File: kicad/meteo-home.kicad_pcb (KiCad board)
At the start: 2 copper layers, 37.5 x 51.4 mm, 14 parts, among them U1 WeMos_D1_mini, U2 SGP30

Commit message: Better connection process control
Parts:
- removed REF** (x4): MountingHole_2.2mm_M2, Mounting_Holes:MountingHole_2.2mm_M2
- moved U2 8.22 mm to (132.2, 96.6), turned to 90 degrees
- moved DHT22 2.09 mm to (121.8, 95.6), turned to 0 degrees
- moved R4 1.70 mm to (110.8, 91.8)
- renumbered D3 to G, D1 to R, D2 to Y
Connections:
- U2 pad 3: Net-(U1-Pad14) -> Net-(U1-Pad13)
- U2 pad 4: Net-(U1-Pad13) -> Net-(U1-Pad14)
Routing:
- net Net-(R4-Pad2): track 63.6 -> 74.3 mm
- net /5V: track 20.9 -> 14.4 mm
- net Net-(U1-Pad14): track 12.5 -> 17.4 mm
- net Net-(U1-Pad13): track 12.5 -> 16.1 mm
- net /3.3V: track 42.8 -> 39.7 mm
- net /GND: track 95.5 -> 96.3 mm
- removed copper zone on B.Cu, net /GND
- removed copper zone on F.Cu, net /GND
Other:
- board text added: "CO2 Detector https://github.com/deuteros76/co2-detector"
- board text removed: "Meteo-home https://github.com/deuteros76/meteo-home"

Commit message: fix: board updated to the last one used in co2-detector
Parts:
- added REF**: MountingHole_2.2mm_M2, Mounting_Holes:MountingHole_2.2mm_M2, F.Cu at (138.0, 93.2)
- added REF**: MountingHole_2.2mm_M2, Mounting_Holes:MountingHole_2.2mm_M2, F.Cu at (139.4, 52.4)
- added REF**: MountingHole_2.2mm_M2, Mounting_Holes:MountingHole_2.2mm_M2, F.Cu at (107.6, 52.4)
- moved U2 1.72 mm to (131.2, 98.0)
- moved DHT22 1.60 mm to (120.2, 95.6)
- moved R4 0.60 mm to (110.2, 91.8)
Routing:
- net /3.3V: track 39.7 -> 53.1 mm
- net Net-(R4-Pad2): track 74.3 -> 61.5 mm
- net /GND: track 96.3 -> 85.9 mm
- net Net-(U1-Pad14): track 17.4 -> 15.8 mm
- net Net-(U1-Pad13): track 16.1 -> 15.1 mm
- added copper zone on B.Cu, net /GND
- added copper zone on F.Cu, net /GND
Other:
- board text added: "CO2 Detector Rev 2 https://github.com/deuteros76/co2-detector"
- board text removed: "CO2 Detector https://github.com/deuteros76/co2-detector"

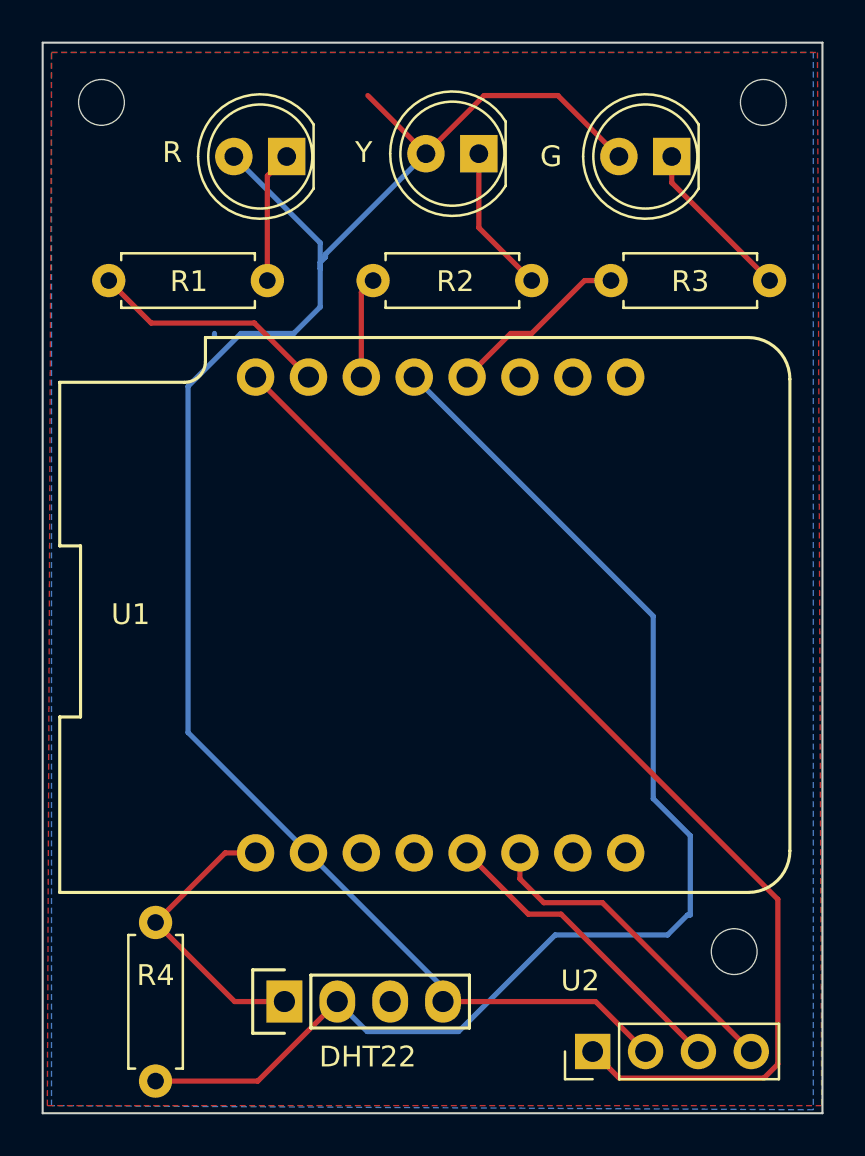
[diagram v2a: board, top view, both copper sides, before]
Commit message: fix: allow deep sleep conecting RST and D0
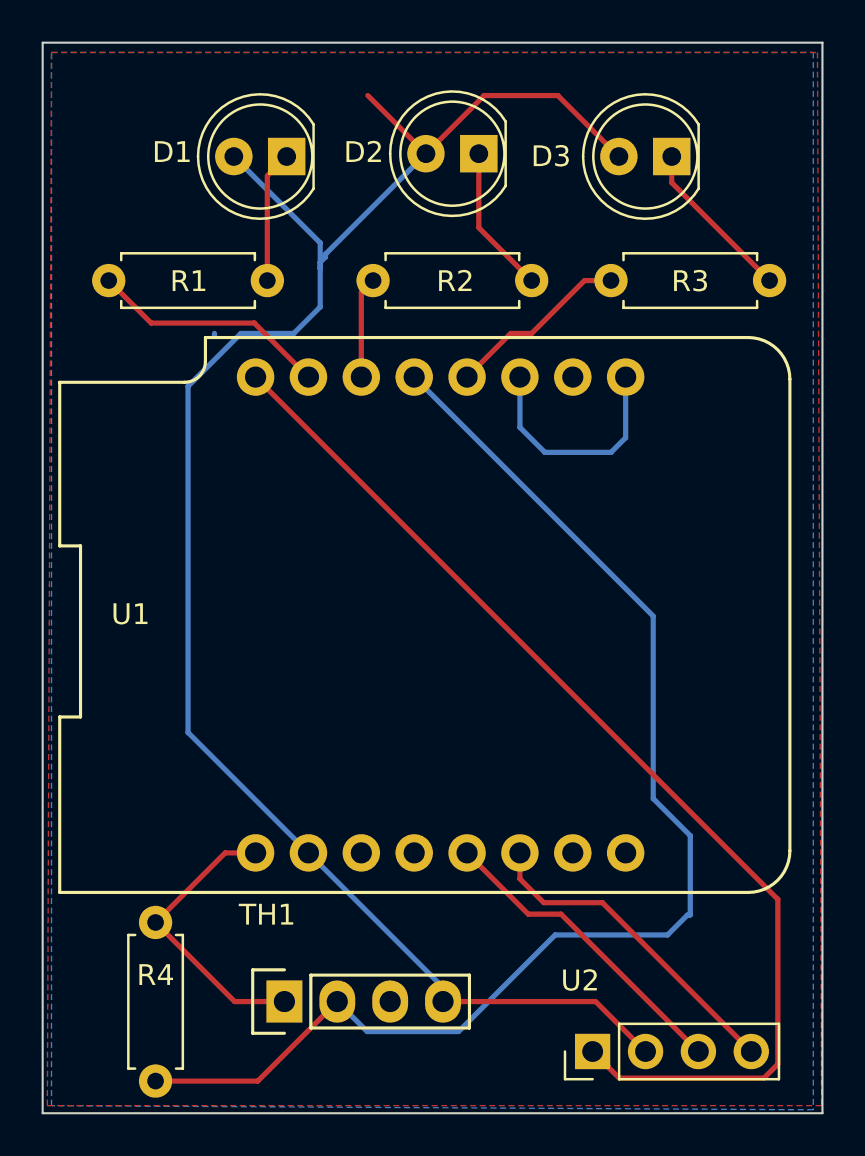
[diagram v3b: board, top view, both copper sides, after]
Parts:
- removed REF** (x3): MountingHole_2.2mm_M2, Mounting_Holes:MountingHole_2.2mm_M2
- TH1: renamed from DHT22; value DHT22_Temperature_Humidity -> DHT22
- renumbered R to D1, Y to D2, G to D3
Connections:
- TH1 pad 3: Net-(TH1-Pad3) -> (no net)
- U1 pad 11: Net-(U1-Pad11) -> (no net)
- U1 pad 12: Net-(U1-Pad12) -> (no net)
- U1 pad 15: Net-(U1-Pad15) -> (no net)
- U1 pad 16: Net-(U1-Pad16) -> (no net)
- U1 pad 2: Net-(U1-Pad2) -> (no net)
- U1 pad 3: Net-(U1-Pad3) -> Net-(U1-Pad1)
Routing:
- net Net-(U1-Pad1): track 0.00 -> 11.2 mm

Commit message: feat: adding labels to the sensors holes
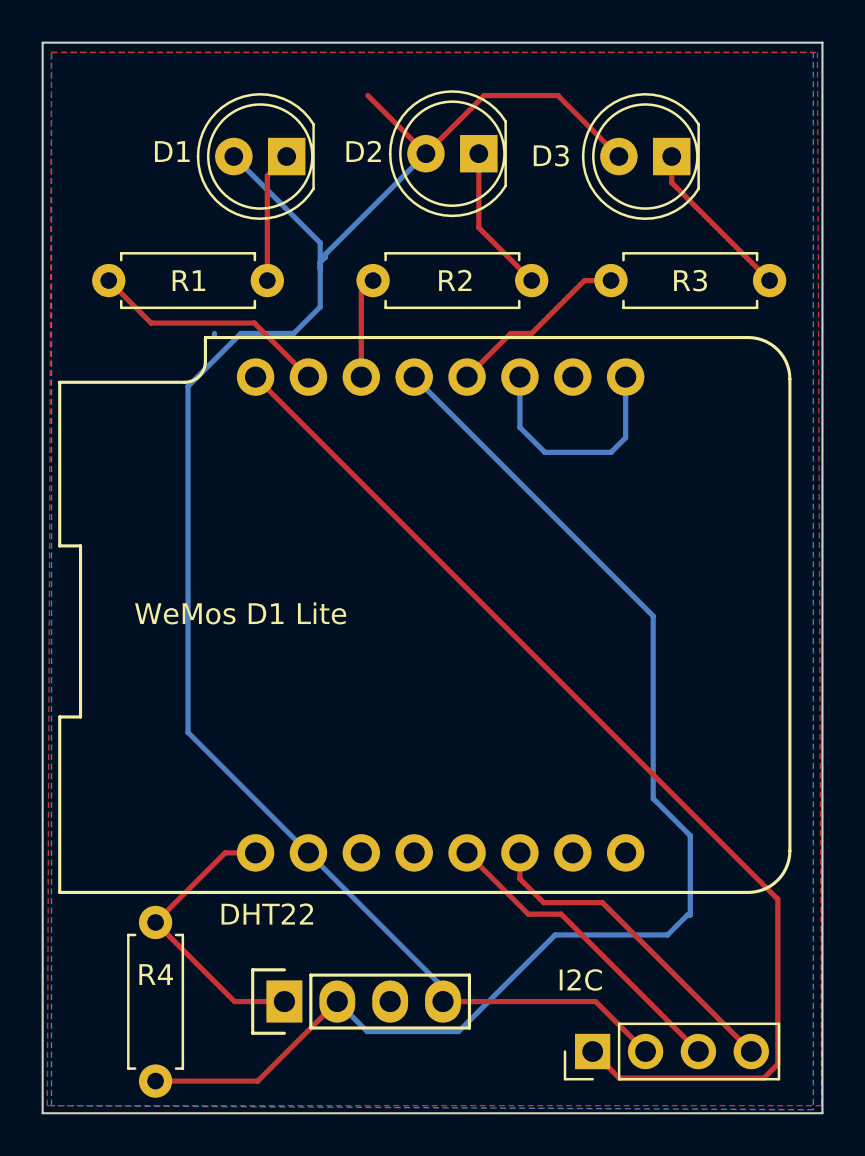
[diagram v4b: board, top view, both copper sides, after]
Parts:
- WeMos D1 Lite: renamed from U1
- renumbered TH1 to DHT22, U2 to I2C
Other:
- net class Default removed
- net class PWR removed
- board text added: "3.3V"
- board text added: "5v"
- board text added: "DATA"
- board text added: "GND"
- board text added: "MeteoHome Rev 3 https://github.com/deuteros76/meteo-home"
- board text added: "SCL"
- board text added: "SDA"
- board text removed: "CO2 Detector Rev 2 https://github.com/deuteros76/co2-detector"
